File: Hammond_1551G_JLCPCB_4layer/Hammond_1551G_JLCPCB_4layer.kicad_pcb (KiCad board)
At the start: 4 copper layers, 44 x 29 mm, 4 parts

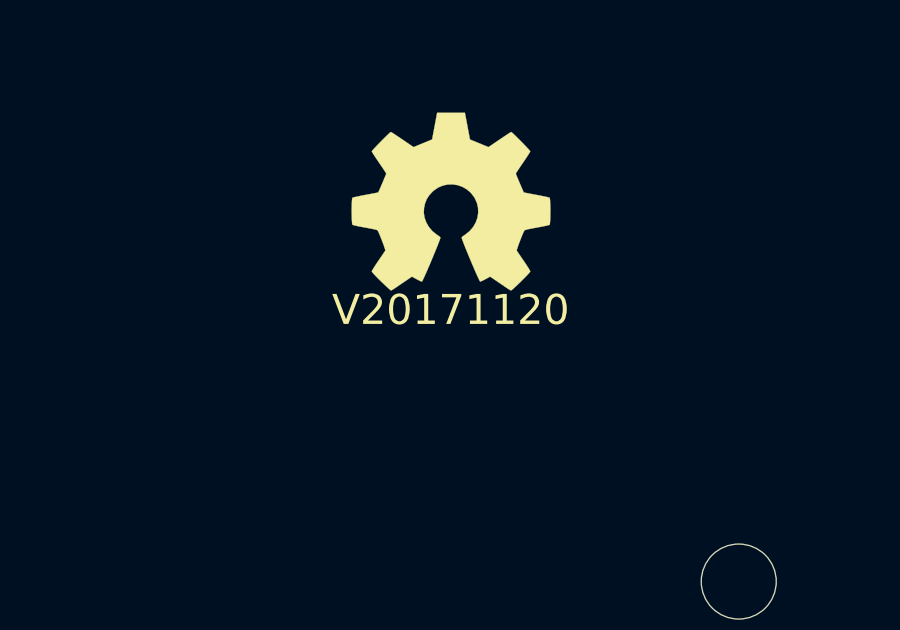
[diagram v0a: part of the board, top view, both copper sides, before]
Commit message: updated Hammond 1551G JLCPCB 4 layer template
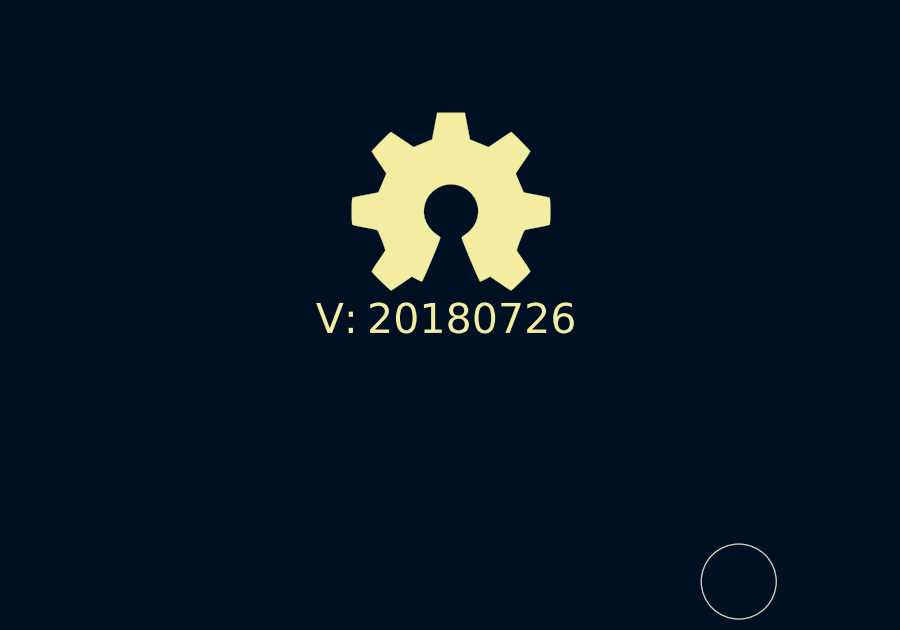
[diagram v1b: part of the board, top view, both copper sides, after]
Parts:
- N2: value V20171120 -> 20180726
- moved N2 1.17 mm to (151.5, 103.1)
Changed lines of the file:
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@@
-(kicad_pcb (version 4) (host pcbnew 4.0.7-e2-6376~61~ubuntu18.04.1)
+(kicad_pcb (version 20171130) (host pcbnew 5.0.0-fee4fd1~65~ubuntu18.04.1)
   (general
-    (links 0)
-    (no_connects 0)
-    (area 127.924999 85.424999 172.075001 114.575001)
     (thickness 1.6)
     (drawings 10)
@@
       (layerselection 0x00030_80000001)
       (usegerberextensions false)
+      (usegerberattributes false)
+      (usegerberadvancedattributes false)
+      (creategerberjobfile false)
       (excludeedgelayer true)
       (linewidth 0.100000)
@@
       (hpglpennumber 1)
       (hpglpenspeed 20)
-      (hpglpendiameter 15)
-      (hpglpenoverlay 2)
+      (hpglpendiameter 15.000000)
       (psnegative false)
       (psa4output false)
@@
       (xy 0.555814 -2.531069)) (layer F.SilkS) (width 0.01))
   )
-  (module SquantorLabels:Label_version (layer F.Cu)
-    (at 150.4 102.7)
-    (fp_text reference N2 (at 0 2) (layer F.Fab) hide
-      (effects (font (size 1 1) (thickness 0.15)))
-    )
-    (fp_text value V20171120 (at 0 0) (layer F.SilkS)
-      (effects (font (size 1 1) (thickness 0.15)))
-    )
-  )
   (module SquantorPcbOutline:MountingHole_2.5mm_no_metal locked (layer F.Cu)
     (at 140 88.25)
@@
     (pad "" np_thru_hole circle (at 0 0) (size 2.5 2.5) (drill 2.5) (layers *.Cu *.Mask))
   )
+  (module SquantorLabels:Label_version (layer F.Cu)
+    (at 151.5 103.1)
+    (fp_text reference N2 (at 0 1.4) (layer F.Fab) hide
+      (effects (font (size 1 1) (thickness 0.15)))
+    )
+    (fp_text value 20180726 (at -0.4 -0.1) (layer F.SilkS)
+      (effects (font (size 1 1) (thickness 0.15)))
+    )
+    (fp_text user V: (at -4.9 -0.1) (layer F.SilkS)
+      (effects (font (size 1 1) (thickness 0.15)))
+    )
+  )
   (gr_line (start 165.75 88.75) (end 165.75 85.5) (layer Edge.Cuts) (width 0.15))

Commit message: updated project to kicad 6
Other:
- net class Default removed
